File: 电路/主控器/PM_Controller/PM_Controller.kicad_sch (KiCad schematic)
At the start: 132 parts, among them J1 Conn_01x04_Socket, J10 Conn_02x04_Odd_Even, J11 Conn_02x06_Odd_Even, J2 Conn_01x04_Socket, J3 Conn_01x04_Socket, J4 Conn_01x04_Socket, J5 Conn_01x02_Pin, J6 Conn_01x02_Pin, J7 Conn_02x04_Odd_Even, J8 Conn_01x04_Pin, J9 Conn_01x04_Socket, P3V3 SolderJumper_2_Open, Q2 AO3400A, Q3 AO3400A, Q5 AO3400A, Q6 AO3400A, U1 AT24CS08-SSHM, U10 TMP102xxDRL, U11 TPS2552DDBVR, U12 TLP127, U13 TLV61048DBVR, U2 AMS1117-3.3, U3 STM32G431RBTx, U5 BQ21040DBV, U6 TPS2552DDBVR, U7 STM32L011D4Px, U8 ME6211C25M5, U9 AT24CS08-SSHM, Y1 32.768kHz, Y2 24Mhz

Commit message: 保存主控 Rev2.0 开发快照并更新 Rev3 对焦结构
整理对焦组件目录和依赖，保留 Rev1.3 历史资料，更新结构与 PCB 兼容性说明；排除本地锁文件、调试日志和自动备份。
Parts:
- removed BT1: Battery_Cell, KiCadLib:cr1220, symbol Device:Battery_Cell
- removed C11, C38, C5, C6: 22uf, Capacitor_Tantalum_SMD:CP_EIA-3528-21_Kemet-B_Pad1.50x2.35mm_HandSolder, symbol Device:C_Polarized
- removed C14, C24: 47uf, Capacitor_Tantalum_SMD:CP_EIA-3528-21_Kemet-B_Pad1.50x2.35mm_HandSolder, symbol Device:C_Polarized
- removed C17, C18, C19, C20: 22uf, Capacitor_SMD:C_0603_1608Metric_Pad1.08x0.95mm_HandSolder, symbol Device:C
- removed C21, C23, C26, C28, C29, C30, C31, C33, C36, C37, C7: 100nf, Capacitor_SMD:C_0603_1608Metric_Pad1.08x0.95mm_HandSolder, symbol Device:C
- removed C22, C27, C8: 10uf, Capacitor_SMD:C_0603_1608Metric_Pad1.08x0.95mm_HandSolder, symbol Device:C
- removed C25: 5pf, Capacitor_SMD:C_0603_1608Metric_Pad1.08x0.95mm_HandSolder, symbol Device:C
- removed C32, C34, C35: 1uf, Capacitor_SMD:C_0603_1608Metric_Pad1.08x0.95mm_HandSolder, symbol Device:C
- removed C39: 22uf, Capacitor_Tantalum_SMD:CP_EIA-3528-21_Kemet-B_HandSolder, symbol Device:C_Polarized
- removed C4: 100nf, Capacitor_SMD:C_0603_1608Metric, symbol Device:C
- removed C40: 1uf, Capacitor_SMD:C_1206_3216Metric_Pad1.33x1.80mm_HandSolder, symbol Device:C
- removed C41: 10uf, Capacitor_SMD:C_1206_3216Metric_Pad1.33x1.80mm_HandSolder, symbol Device:C
- removed CHG1, PW_LED1: LED, LED_SMD:LED_0805_2012Metric_Pad1.15x1.40mm_HandSolder, symbol Device:LED
- removed D1: SS34, Diode_SMD:D_SMA, symbol Diode:SS34
- removed D3: SS32, Diode_SMD:D_SMA_Handsoldering, symbol Diode:SS32
- removed D4: 1N5819WS, Diode_SMD:D_SOD-323_HandSoldering, symbol Diode:1N5819WS
- removed FB1: FerriteBead, Inductor_SMD:L_0805_2012Metric_Pad1.05x1.20mm_HandSolder, symbol Device:FerriteBead
- removed FLASH1: Conn_01x02_Pin, Connector_Wire:SolderWire-0.1sqmm_1x02_P3.6mm_D0.4mm_OD1mm_Relief, symbol Connector:Conn_01x02_Pin
- removed H1, H2, H3, H4: MountingHole, MountingHole:MountingHole_3.2mm_M3, symbol Mechanical:MountingHole
- removed H5, H6, H7, H8, H9: MountingHole_Pad, MountingHole:MountingHole_3.2mm_M3_DIN965_Pad_TopBottom, symbol Mechanical:MountingHole_Pad
- removed J1, J4: Conn_01x04_Socket, Connector_JST:JST_PH_S4B-PH-K_1x04_P2.00mm_Horizontal, symbol Connector:Conn_01x04_Socket
- removed J10, J7: Conn_02x04_Odd_Even, Connector_PinHeader_1.27mm:PinHeader_2x04_P1.27mm_Vertical, symbol Connector_Generic:Conn_02x04_Odd_Even
- removed J11: Conn_02x06_Odd_Even, Connector_PinHeader_1.27mm:PinHeader_2x06_P1.27mm_Vertical, symbol Connector_Generic:Conn_02x06_Odd_Even
- removed J2, J3, J9: Conn_01x04_Socket, Connector_PinHeader_2.54mm:PinHeader_1x04_P2.54mm_Vertical, symbol Connector:Conn_01x04_Socket
- removed J5: Conn_01x02_Pin, Connector_Wire:SolderWire-0.5sqmm_1x02_P4.8mm_D0.9mm_OD2.3mm, symbol Connector:Conn_01x02_Pin
- removed J6: Conn_01x02_Pin, Connector_PinSocket_2.00mm:PinSocket_1x02_P2.00mm_Vertical, symbol Connector:Conn_01x02_Pin
- removed J8: Conn_01x04_Pin, Connector_PinHeader_2.00mm:PinHeader_1x04_P2.00mm_Vertical, symbol Connector:Conn_01x04_Pin
- removed JP1, JP2: SolderJumper_3_Bridged12, Jumper:SolderJumper-3_P1.3mm_Bridged12_Pad1.0x1.5mm, symbol Jumper:SolderJumper_3_Bridged12
- removed L2, L3: 4.7uH, Inductor_SMD:L_APV_APH0650, symbol Device:L
- removed NRST1, NRST2, P3V3: SolderJumper_2_Open, Jumper:SolderJumper-2_P1.3mm_Open_RoundedPad1.0x1.5mm, symbol Jumper:SolderJumper_2_Open
- removed Q2, Q3, Q5, Q6: AO3400A, Package_TO_SOT_SMD:SOT-23, symbol Transistor_FET:AO3400A
- removed R12, R14, R15, R2, R23, R24, R27, R28, R31, R39, R41, R42, R8: 100k, Resistor_SMD:R_0603_1608Metric_Pad0.98x0.95mm_HandSolder, symbol Device:R
- removed R13: 1.5k, Resistor_SMD:R_0603_1608Metric_Pad0.98x0.95mm_HandSolder, symbol Device:R
- removed R16, R17, R18, R20, R21, R22: 100k(NC), Resistor_SMD:R_0603_1608Metric_Pad0.98x0.95mm_HandSolder, symbol Device:R
- removed R25, R26, R32, R40, R6: 1k, Resistor_SMD:R_0603_1608Metric_Pad0.98x0.95mm_HandSolder, symbol Device:R
- removed R29, R33, R34, R35, R36, R45, R7: 10k, Resistor_SMD:R_0603_1608Metric_Pad0.98x0.95mm_HandSolder, symbol Device:R
- removed R30, R38, R43: 150k, Resistor_SMD:R_0603_1608Metric_Pad0.98x0.95mm_HandSolder, symbol Device:R
- removed R37: 22k, Resistor_SMD:R_0603_1608Metric_Pad0.98x0.95mm_HandSolder, symbol Device:R
- removed R44: 33k, Resistor_SMD:R_0603_1608Metric_Pad0.98x0.95mm_HandSolder, symbol Device:R
- removed U1, U9: AT24CS08-SSHM, Package_SO:SOIC-8_3.9x4.9mm_P1.27mm, symbol Memory_EEPROM:AT24CS08-SSHM
- removed U10: TMP102xxDRL, Package_TO_SOT_SMD:SOT-563, symbol Sensor_Temperature:TMP102xxDRL
- removed U11, U6: TPS2552DDBVR, DBV0006A_TEX, symbol TPS2552d:TPS2552DDBVR
- removed U12: TLP127, Package_SO:MFSOP6-4_4.4x3.6mm_P1.27mm, symbol Isolator:TLP127
- removed U13: TLV61048DBVR, SOT-23-6_DBV_TEX, symbol 2025-04-10_12-12-53:TLV61048DBVR
- removed U2: AMS1117-3.3, Package_TO_SOT_SMD:SOT-223-3_TabPin2, symbol Regulator_Linear:AMS1117-3.3
- removed U3: STM32G431RBTx, Package_QFP:LQFP-64_10x10mm_P0.5mm, symbol MCU_ST_STM32G4:STM32G431RBTx
- removed U5: BQ21040DBV, Package_TO_SOT_SMD:SOT-23-6_Handsoldering, symbol Battery_Management:BQ21040DBV
- removed U7: STM32L011D4Px, Package_SO:TSSOP-14_4.4x5mm_P0.65mm, symbol MCU_ST_STM32L0:STM32L011D4Px
- removed U8: ME6211C25M5, Package_TO_SOT_SMD:SOT-23-5_HandSoldering, symbol Regulator_Linear:ME6211C25M5
- removed Y1: 32.768kHz, Crystal:Crystal_C26-LF_D2.1mm_L6.5mm_Horizontal, symbol Device:Crystal
- removed Y2: 24Mhz, Crystal:Crystal_DS26_D2.0mm_L6.0mm_Horizontal, symbol Device:Crystal
- added C11: 100nf, Capacitor_SMD:C_0603_1608Metric, symbol Device:C
- added C13, C14: 22uf, Capacitor_SMD:C_0603_1608Metric, symbol Device:C
- added C9: 10uf, Capacitor_SMD:C_0805_2012Metric, symbol Device:C
- added U1: ESP32-S3-WROOM-1, RF_Module:ESP32-S3-WROOM-1, symbol RF_Module:ESP32-S3-WROOM-1
- added U2: STM32G030K8Tx, Package_QFP:LQFP-32_7x7mm_P0.8mm, symbol MCU_ST_STM32G0:STM32G030K8Tx
- added U3: PCF85263AT, Package_SO:SOIC-8_3.9x4.9mm_P1.27mm, symbol Timer_RTC:PCF85263AT
- added U4: TPS563201, Package_TO_SOT_SMD:SOT-23-6, symbol Regulator_Switching:TPS563201
- C1, C2: value 5pf -> 1uf; footprint Capacitor_SMD:C_0603_1608Metric_Pad1.08x0.95mm_HandSolder -> Capacitor_SMD:C_0603_1608Metric
- C10: value 1uf -> 10uf; footprint Capacitor_SMD:C_0603_1608Metric_Pad1.08x0.95mm_HandSolder -> Capacitor_SMD:C_0805_2012Metric
- C12: footprint Capacitor_SMD:C_1206_3216Metric_Pad1.33x1.80mm_HandSolder -> Capacitor_SMD:C_0603_1608Metric
- C3: value 5pf -> 22uf; footprint Capacitor_SMD:C_0603_1608Metric_Pad1.08x0.95mm_HandSolder -> Capacitor_SMD:C_0805_2012Metric
- L1: value 4.7uH -> 2.2uH; footprint Inductor_SMD:L_APV_APH0650 -> Inductor_SMD:L_Coilcraft_1008HQ_2520Metric
- R1: value 100k -> 10k; footprint Resistor_SMD:R_0603_1608Metric_Pad0.98x0.95mm_HandSolder -> Resistor_SMD:R_0603_1608Metric
- R3: value RPORG(1k) -> 10k; footprint Resistor_SMD:R_0603_1608Metric_Pad0.98x0.95mm_HandSolder -> Resistor_SMD:R_0603_1608Metric
- R4: value 1.5k -> 10k; footprint Resistor_SMD:R_0603_1608Metric_Pad0.98x0.95mm_HandSolder -> Resistor_SMD:R_0603_1608Metric
- R5: value 22k -> 33.2k; footprint Resistor_SMD:R_0603_1608Metric_Pad0.98x0.95mm_HandSolder -> Resistor_SMD:R_0603_1608Metric
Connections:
- net +BATT is gone; now on net GND: R4.2
- net HSE+ is gone; now on net GND: C3.1
- net LSE+ is gone; now on net GND: C1.1
- net LSE- is gone; now on net GND: C2.1
- net +3.3V: now also C2.2, C3.2, R1.2, U1.2 (3V3); no longer C12.1
- net GND: now also C13.2, C14.2, C9.2, U1.1 (GND), U1.40 (GND), U1.41 (GND), U2.5 (VSS), U4.1 (GND); no longer C1.2, C2.2, C3.2, R1.2, R3.2, R5.2
- net at R3.1: now also U4.5 (EN)
- net +3V3: now reaches L1.2
- net +3V3: now also C12.1, R5.1, C13.1, C14.1
- net at R4.1: now also R5.2, U4.4 (VFB)
- net +5VA renamed +6V
- net +6V: now also R3.2, C9.1, U4.3 (VIN)
- net BAT_OUT: no longer names the net of L1.1
- net BAT_OUT: now also C11.1, U4.2 (SW)
- net _C2P1_ renamed ESP_EN
- net ESP_EN: now also C1.2, U1.3 (EN)
- new net: C11.2, U4.6 (VBST)
- new net ESP _RXD0: U1.36 (RXD0)
- new net ESP _TXD0: U1.37 (TXD0)
- new net ESP_BOOT: U1.27 (IO0)
- no-connect marks 13 -> 3
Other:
- note removed: "EEPROM"
- note removed: "G474RETx 应该可用"
- note removed: "LDO"
- note removed: "上下拉"
- note removed: "接口"
- note removed: "接口电平"
- note removed: "温度"
- note removed: "电池充电、升压"
- note removed: "电源管理"
- note removed: "相机功能"
- note removed: "预留电源输出"
- title: PM Controller （最初投产版本） -> PM Controller

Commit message: 主控器与CubeMX配置一致
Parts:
- added R12: 1k, Resistor_SMD:R_0603_1608Metric, symbol Device:R
- added R2: 4.7k, Resistor_SMD:R_0603_1608Metric, symbol Device:R
- added U5: DRV8251ADDAR, EasyEDA:SOPOWERPAD-8_L4.9-W3.9-P1.27-LS6.0-TL-EP, symbol EasyEDA:DRV8251ADDAR
- added U6, U7: 74HC165, Package_SO:SOIC-16_3.9x9.9mm_P1.27mm, symbol 74xx:74HC165
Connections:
- net +3V3 is gone; now on net +3.3V: C12.1, C13.1, C14.1, L1.2, R5.1
- net +3.3V: now also U2.4 (VDD), U5.4 (VREF), U6.16 (VCC), U7.16 (VCC)
- net +6V: now also U5.5 (VM)
- net GND: now also U3.4 (VSS), R2.2, U5.7 (GND), U5.9 (PAD), U6.8 (GND), U7.8 (GND)
- net ESP_TXD1: now reaches U1.10 (IO17)
- net ESP_RXD1: now reaches U1.11 (IO18)
- net ESP_UD-: now reaches U1.13 (USB_D-)
- net ESP_UD+: now reaches U1.14 (USB_D+)
- net LCD_RES: now reaches U1.17 (IO9)
- net LCD_DC: now reaches U1.18 (IO10)
- net LCD_BLK: now reaches U1.19 (IO11)
- net LCD_MOSI: now reaches U1.20 (IO12)
- net LCD_CLK: now reaches U1.21 (IO13)
- net LCD_CS: now reaches U1.22 (IO14)
- net MASPI_MOSI: now reaches U1.31 (IO38)
- net MASPI_MOSI: now also U2.14 (PA7)
- net MASPI_MISO: now reaches U1.32 (IO39)
- net MASPI_MISO: now also U2.13 (PA6)
- net MASPI_CLK: now reaches U1.33 (IO40)
- net MASPI_CLK: now also U2.12 (PA5)
- net MASPI_CS: now reaches U1.34 (IO41)
- net MASPI_CS: now also U2.11 (PA4)
- net ESP_TXD2: now reaches U1.4 (IO4)
- net ESP_RXD2: now reaches U1.5 (IO5)
- net STM_SPI2_CS: now reaches U2.1 (PB9)
- net STM_TXD1: now reaches U2.22 (PA9/PA11)
- net STM_RXD1: now reaches U2.23 (PA10/PA12)
- net STM_SWDIO: now reaches U2.24 (PA13)
- net STM_SWCLK: now reaches U2.25 (PA14)
- net MotorPWM_A: now reaches U2.28 (PB4)
- net MotorPWM_A: now also U5.3 (IN1)
- net MotorIN2: now reaches U2.29 (PB5)
- net MotorIN2: now also U5.2 (IN2)
- net STM_SPI2_MISO: now reaches U2.30 (PB6)
- net STM_SPI2_MOSI: now reaches U2.31 (PB7)
- net STM_SPI2_CLK: now reaches U2.32 (PB8)
- net STM_NRST: now reaches U2.6 (NRST)
- net ESP _RXD0 renamed ESP_RXD0
- net ESP _TXD0 renamed ESP_TXD0
- new net: R12.2, R2.1, U5.1 (IPROPI)
- new net ADC_MT: R12.1
- new net MOT_A: U5.6 (OUT1)
- new net MOT_B: U5.8 (OUT2)
- no-connect marks 3 -> 5
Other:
- note added: "TIM3_CH1 TIM3_CH2"
- moved on the sheet: U2

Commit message: 更新 PM Controller Rev2.0 电路与四层 PCB 设计
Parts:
- removed U2: STM32G030K8Tx, Package_QFP:LQFP-32_7x7mm_P0.8mm, symbol MCU_ST_STM32G0:STM32G030K8Tx
- removed U3: PCF85263AT, Package_SO:SOIC-8_3.9x4.9mm_P1.27mm, symbol Timer_RTC:PCF85263AT
- removed U7: 74HC165, Package_SO:SOIC-16_3.9x9.9mm_P1.27mm, symbol 74xx:74HC165
- added C15, C27, C31: 100nF, Capacitor_SMD:C_0603_1608Metric, symbol Device:C
- added C16: 1nf, Capacitor_SMD:C_0603_1608Metric, symbol Device:C
- added C17, C18, C21, C4: 1uf, Capacitor_SMD:C_0603_1608Metric, symbol Device:C
- added C19, C20, C24, C28: 100nf, Capacitor_SMD:C_0603_1608Metric, symbol Device:C
- added C22, C23, C29, C30: 10uf, Capacitor_SMD:C_0805_2012Metric, symbol Device:C
- added C25, C26: 22uf, Capacitor_SMD:C_0603_1608Metric, symbol Device:C
- added C5, C6: DNP, Capacitor_SMD:C_0603_1608Metric, symbol Device:C
- added C7: 220uf, Capacitor_Tantalum_SMD:CP_EIA-7343-31_Kemet-D, symbol Device:C_Polarized
- added C8: TBD(1uf), Capacitor_SMD:C_0603_1608Metric, symbol Device:C
- added FPC1: AFC01-S08FCA-00, EasyEDA:FPC-SMD_P0.50-8P_FGS-XJ-H2.0, symbol EasyEDA:AFC01-S08FCA-00
- added FPC2: AFC11-S08ICA-00, EasyEDA:CONN-TH-8P_AFC11-S08ICA-00, symbol EasyEDA:AFC11-S08ICA-00
- added H1, H2, H3: WAFER-PH2.0-2PWB, EasyEDA:CONN-SMD_2P-P2.00_XUNPU_WAFER-PH2.0-2PWB, symbol EasyEDA:WAFER-PH2.0-2PWB
- added H4, H5, H6, H7: MountingHole, MountingHole:MountingHole_3.2mm_M3_DIN965_Pad, symbol Mechanical:MountingHole
- added J1: Conn_01x04_Pin, Connector_PinHeader_1.27mm:PinHeader_1x04_P1.27mm_Vertical, symbol Connector:Conn_01x04_Pin
- added JP1: SolderJumper_2_Bridged, Jumper:SolderJumper-2_P1.3mm_Bridged2Bar_RoundedPad1.0x1.5mm, symbol Jumper:SolderJumper_2_Bridged
- added L2: 3.3uH, Inductor_SMD:L_Changjiang_FXL0530, symbol Device:L
- added Q1, Q2: FDV301N, Package_TO_SOT_SMD:SOT-23, symbol Transistor_FET:Q_NMOS_GSD
- added Q3: SS8550, Package_TO_SOT_SMD:SOT-23, symbol Transistor_BJT:SS8550
- added R10, R14, R19, R20, R21, R23, R24, R31, R32, R33, R34, R35, R36, R37, R38, R50, R56, R6, R9: 10k, Resistor_SMD:R_0603_1608Metric, symbol Device:R
- added R11, R13: 100, Resistor_SMD:R_0603_1608Metric, symbol Device:R
- added R15, R16: 4.7k, Resistor_SMD:R_0603_1608Metric, symbol Device:R
- added R17: 10, Resistor_SMD:R_0603_1608Metric, symbol Device:R
- added R18, R57: 1k, Resistor_SMD:R_0603_1608Metric, symbol Device:R
- added R22: 68.1k, Resistor_SMD:R_0603_1608Metric, symbol Device:R
- added R25: 390, Resistor_SMD:R_0603_1608Metric, symbol Device:R
- added R26, R27: 5.1k, Resistor_SMD:R_0603_1608Metric, symbol Device:R
- added R28, R29: 0, Resistor_SMD:R_0603_1608Metric, symbol Device:R
- added R30: 2.1k (RPROG), Resistor_SMD:R_0603_1608Metric, symbol Device:R
- added R47, R48, R49: 499, Resistor_SMD:R_0603_1608Metric, symbol Device:R
- added R58: 10.1k, Resistor_SMD:R_0603_1608Metric, symbol Device:R
- added R59: 680, Resistor_SMD:R_0603_1608Metric, symbol Device:R
- added R7, R8: 100k, Resistor_SMD:R_0603_1608Metric, symbol Device:R
- added SW1, SW2, SW3, SW4, SW5: TS-1088R-02026, EasyEDA:SW-SMD_L3.9-W3.0-P4.45, symbol EasyEDA:TS-1088R-02026
- added U10: TPS7A0233PDBVR, EasyEDA:SOT-23-5_L2.9-W1.6-P0.95-LS2.8-BR, symbol EasyEDA:TPS7A0233PDBVR
- added U11: SN74AUP1G17DBVR, EasyEDA:SOT-23-5_L3.0-W1.7-P0.95-LS2.8-BR, symbol EasyEDA:SN74AUP1G17DBVR
- added U12: 24C64, Package_TO_SOT_SMD:SOT-23-5, symbol Memory_EEPROM:AT24CS16-STUM
- added U13: ZX-ZH1.5-3PWT, EasyEDA:CONN-SMD_3P-P1.50_ZX-ZH1.5-3PWT, symbol EasyEDA:ZX-ZH1.5-3PWT
- added U14: TPS563201, Package_TO_SOT_SMD:SOT-23-6, symbol Regulator_Switching:TPS563201
- added U15, U9: ZX-ZH1.5-4PWT, EasyEDA:CONN-SMD_4P-P1.50_ZX-ZH1.5-4PWT, symbol EasyEDA:ZX-ZH1.5-4PWT
- added U16: TLP291, Package_SO:SOIC-4_4.55x2.6mm_P1.27mm, symbol Isolator:TLP291
- added U18: TPS3808G01DBVR, Package_TO_SOT_SMD:SOT-23-6, symbol Power_Supervisor:TPS3808DBV
- added U19: ZX-ZH1.5-5PWT, EasyEDA:CONN-SMD_5P-P1.50_ZX-ZH1.5-5PWT, symbol EasyEDA:ZX-ZH1.5-5PWT
- added U2: TP4057, Package_TO_SOT_SMD:TSOT-23-6, symbol Battery_Management:TP4057
- added U3: SN74AUP1G74DCUR, EasyEDA:VSSOP-8_L2.1-W2.4-P0.50-LS3.2-BR, symbol EasyEDA:SN74AUP1G74DCUR
- added U7: USBLC6-2SC6, Package_TO_SOT_SMD:SOT-23-6, symbol Power_Protection:USBLC6-2SC6
- added U8: ZX-XH2.54-5PWT, EasyEDA:CONN-SMD_5P-P2.54_MEGASTAR_ZX-XH2.54-5PWT, symbol EasyEDA:ZX-XH2.54-5PWT
- added USB1: MC-402L68, EasyEDA:USB-C-SMD_MC-402L68, symbol EasyEDA:MC-402L68
- R12: value 1k -> 0
- R2: value 4.7k -> 1k
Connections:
- net +3.3V: now also C15.1, C27.1, C31.1, C4.2, FPC1.2, FPC2.7, J1.1 (Pin_1), Q3.2 (E), R15.2, R16.2, R19.1, R23.2, R31.1, R32.1, R33.1, R34.1, R35.1, R36.1, R37.1, R38.1, R50.2, R56.2, R6.1, R9.2, U12.4 (VCC), U18.6 (VDD), U19.1, U9.1
- net +6V: now also C25.1, C26.1, C28.1, C7.1, L2.2, R22.1; no longer C10.1, C9.1, R3.2, U4.3 (VIN)
- net ADC_MT: now also U1.12 (IO8), C8.2
- net ESP_BOOT: now also R50.1, SW4.1
- net ESP_EN: now also SW5.1
- net ESP_RXD0: now also J1.3 (Pin_3)
- net ESP_RXD1: now also U1.5 (IO5), U9.3; no longer U1.11 (IO18)
- net ESP_RXD2: now also U1.10 (IO17), U15.3; no longer U1.5 (IO5)
- net ESP_TXD0: now also J1.2 (Pin_2), R47.1; no longer U1.37 (TXD0)
- net ESP_TXD1: now also R49.2, U9.2; no longer U1.10 (IO17)
- net ESP_TXD2: now also R48.2, U15.2; no longer U1.4 (IO4)
- net ESP_UD+: now also R29.1, U7.3 (I/O2); no longer U1.14 (USB_D+)
- net ESP_UD-: now also R28.1, U7.1 (I/O1); no longer U1.13 (USB_D-)
- net GND: now also U6.10 (DS), U6.15 (~{CE}), C15.2, C16.1, C17.2, C18.2, C19.2, C20.2, C21.2, C22.2, C23.2, C25.2, C26.2, C27.2, C28.2, C29.2, C30.2, C31.2, C4.1, C5.1, C6.1, C7.2, C8.1, FPC1.7, FPC2.2, H2.1, J1.4 (Pin_4), Q1.2 (S), Q2.2 (S), R14.1, R21.2, R24.1, R26.2, R27.2, R30.2, R57.1, R59.1, R7.1, SW1.2, SW2.2, SW3.2, SW4.2, SW5.2, U10.2 (GND), U11.3 (GND), U12.2 (GND), U12.5 (WP), U14.1 (GND), U15.4, U16.2, U18.2 (GND), U19.5, U2.2 (GND), U3.2 (D), U3.4 (GND), U7.2 (GND), U8.4, U8.5, U9.4, USB1.1 (EH), USB1.2 (EH), USB1.3 (EH), USB1.4 (EH), USB1.B1 (GND), USB1.B12 (GND)
- net LCD_BLK: now also U1.17 (IO9), R18.1; no longer U1.19 (IO11)
- net LCD_CLK: now also FPC1.3, FPC2.6
- net LCD_CS: now also FPC1.1, FPC2.8
- net LCD_DC: now also U1.19 (IO11), FPC1.5, FPC2.4; no longer U1.18 (IO10)
- net LCD_MOSI: now also FPC1.4, FPC2.5
- net LCD_RES: now also U1.18 (IO10), FPC1.6, FPC2.3; no longer U1.17 (IO9)
- net MASPI_CLK: now also U6.2 (CP)
- net MASPI_CS: now also U1.32 (IO39), U6.1 (~{PL}), R6.2; no longer U1.34 (IO41)
- net MASPI_MISO: now also U1.34 (IO41), U6.9 (Q7); no longer U1.32 (IO39)
- net MOT_A: now also H1.1
- net MOT_B: now also H1.2
- net MotorIN2: now also U1.38 (IO2)
- net MotorPWM_A: now also U1.39 (IO1)
- net USBPWR_DET: now reaches U1.23 (IO21)
- net USBPWR_DET: now also R56.1, U18.1 (~{RESET})
- net SHUT_TRG: now reaches U1.35 (IO42)
- net SHUT_TRG: now also H2.2, R23.1
- net ESP_FILM_TRG: now reaches U1.6 (IO6)
- net ESP_FILM_TRG: now also Q1.3 (D), R9.1
- net ESP_FILM_CLR: now reaches U1.7 (IO7)
- net ESP_FILM_CLR: now also R11.2, R14.2
- net ESP_SCL: now reaches U1.8 (IO15)
- net ESP_SCL: now also R16.1, U12.1 (SCL)
- net ESP_SDA: now reaches U1.9 (IO16)
- net ESP_SDA: now also R15.1, U12.3 (SDA)
- net ESP_KEY1: now reaches U6.11 (D0)
- net ESP_KEY1: now also R31.2, SW3.1
- net ESP_KEY2: now reaches U6.12 (D1)
- net ESP_KEY2: now also R32.2, SW2.1
- net ESP_KEY3: now reaches U6.13 (D2)
- net ESP_KEY3: now also R33.2, SW1.1
- net ESP_KEY4: now reaches U6.14 (D3)
- net ESP_KEY4: now also R36.2, U19.2
- net ESP_KEY5: now reaches U6.3 (D4)
- net ESP_KEY5: now also R35.2, U19.4
- net ESP_KEY6: now reaches U6.4 (D5)
- net ESP_KEY6: now also R34.2, U19.3
- net BAT_CHG_OD: now reaches U6.5 (D6)
- net BAT_CHG_OD: now also R38.2, U2.1 (~{CHRG})
- net BAT_STB_OD: now reaches U6.6 (D7)
- net BAT_STB_OD: now also R37.2, U2.5 (STDBY)
- net MASPI_MOSI renamed FLASH_TRG
- net FLASH_TRG: now also R24.2, R25.2
- new net: Q3.3 (C), R17.1
- new net: R49.1, U1.4 (IO4)
- new net: C24.1, L2.1, U14.2 (SW)
- new net: R21.1, R22.2, U14.4 (VFB)
- new net: R20.1, U14.5 (EN)
- new net: C24.2, U14.6 (VBST)
- new net: R25.1, U16.1
- new net: R26.1, USB1.A5 (CC1)
- new net: U11.4 (Y), U3.1 (CLK)
- new net: JP1.2 (B), U15.1
- new net: R48.1, U1.11 (IO18)
- new net: R47.2, U1.37 (TXD0)
- new net: Q1.1 (G), R13.2
- new net: Q3.1 (B), R18.2, R19.2
- new net: R27.1, USB1.B5 (CC2)
- new net: R7.2, U13.3
- new net: R8.1, U13.1
- new net: H3.2, U16.3
- new net: H3.1, U16.4
- new net: C16.2, R57.2, R58.1, U18.5 (SENSE)
- new net: R30.1, U2.6 (PROG)
- new net: Q2.1 (G), R11.1
- new net #FILM_KEY_CLR: Q2.3 (D), R10.1, U3.7 (#PRE)
- new net #FILM_TRG: R13.1, U3.5 (Q)
- new net +BATT: C17.1, C30.1, U10.1 (IN), U10.3 (EN), U2.3 (BAT), U8.3
- new net FILM_KEY: C21.1, U11.2 (A), U13.2
- new net LEDA: FPC1.8, FPC2.1, R17.2
- new net VAA: C18.1, C19.1, C20.1, R10.2, R8.2, U10.5 (OUT), U11.5 (VCC), U3.6 (#CLR), U3.8 (VCC)
- new net VBUS: C29.1, R58.2, R59.2, U2.4 (V_{CC}), U7.5 (VBUS), USB1.B4 (VBUS), USB1.B9 (VBUS)
- new net VCC: C10.1, C22.1, C23.1, C9.1, JP1.1 (A), R20.2, R3.2, U14.3 (VIN), U4.3 (VIN), U8.1, U8.2
- new net _1UD+: C6.2, R29.2, U1.14 (USB_D+)
- new net _1UD-: C5.2, R28.2, U1.13 (USB_D-)
- new net _UD+: U7.4 (I/O2), USB1.A6 (DP1)
- new net _UD-: U7.6 (I/O1), USB1.A7 (DN1)
- no-connect marks 5 -> 33
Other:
- note added: "(CPOL=1, CPHA=0), MSB first;"
- note removed: "TIM3_CH1 TIM3_CH2"
- moved on the sheet: C1, C10, C11, C12, C13, C14, C2, C3, C9, L1, R1, R12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

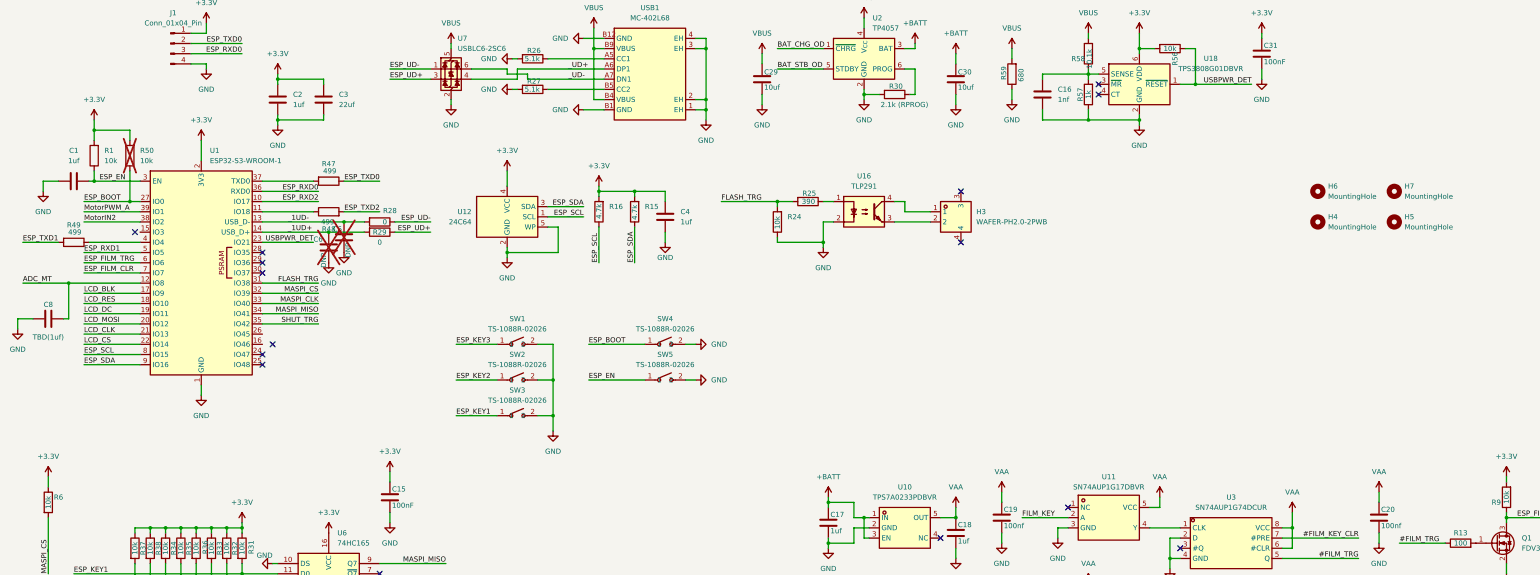
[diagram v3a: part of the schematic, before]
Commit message: 保存 PM_Controller Rev2.0 投产快照及 Rev3 装配更新
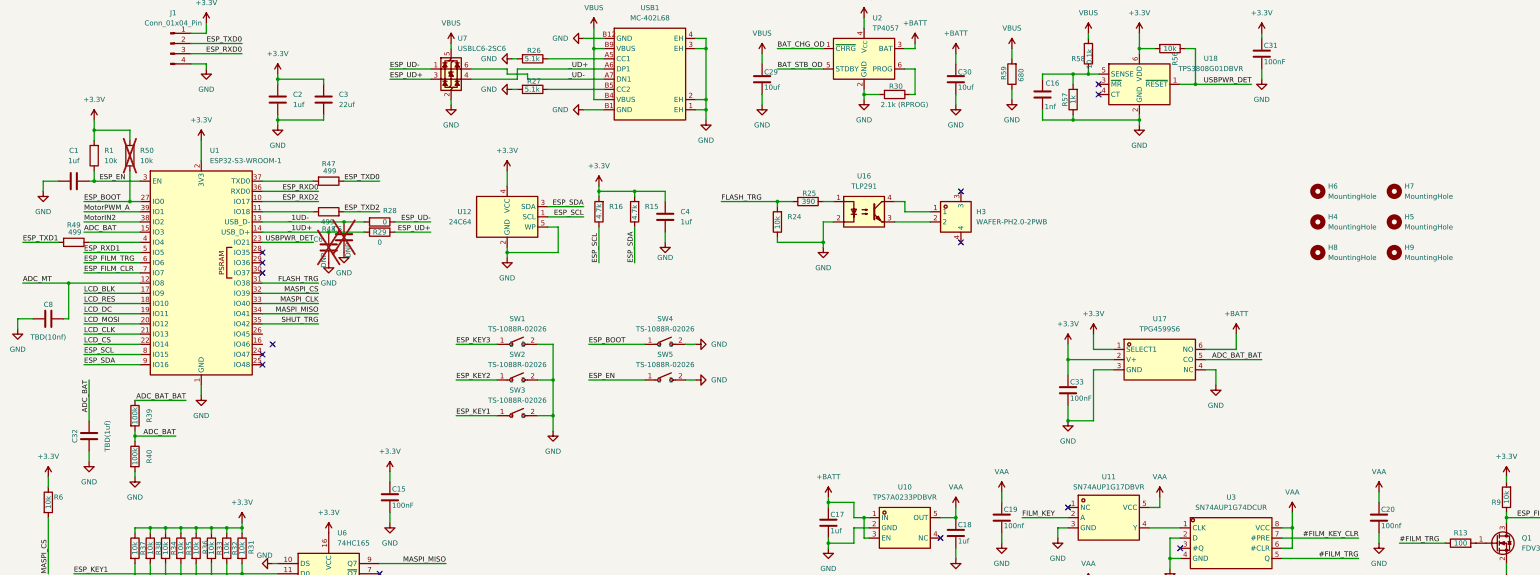
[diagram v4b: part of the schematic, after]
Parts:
- added C32: TBD(1uf), Capacitor_SMD:C_0603_1608Metric, symbol Device:C
- added C33: 100nF, Capacitor_SMD:C_0603_1608Metric, symbol Device:C
- added H8, H9: MountingHole, MountingHole:MountingHole_2.2mm_M2, symbol Mechanical:MountingHole
- added R39, R40: 100k, Resistor_SMD:R_0603_1608Metric, symbol Device:R
- added U17: TPG4599S6, EasyEDA:TSOT-23-6_L2.9-W1.6-P0.95-LS2.8-BL, symbol EasyEDA:TPG4599S6
- C8: value TBD(1uf) -> TBD(10nf)
- H4, H5, H6, H7: footprint MountingHole:MountingHole_3.2mm_M3_DIN965_Pad -> MountingHole:MountingHole_3.2mm_M3
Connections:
- net +3.3V: now also C33.1, U17.1 (SELECT1), U17.2 (V+)
- net +BATT: now also U17.6 (NO)
- net GND: now also C32.1, C33.2, R40.2, U17.3 (GND), U17.4 (NC)
- net ADC_BAT: now reaches U1.15 (IO3)
- net ADC_BAT: now also C32.2, R39.2, R40.1
- new net ADC_BAT_BAT: R39.1, U17.5 (CO)
- no-connect marks 33 -> 32
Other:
- moved on the sheet: R57
